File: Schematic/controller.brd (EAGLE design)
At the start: 100 x 80 mm, 46 parts, among them IC1 LM1117-3V3, IC2 LMV358SOIC, Q1 16MHZ, Q2 MMBT2222A, Q3 FDN740P, U1 MC34063SMD, U2 ATMEGA328P

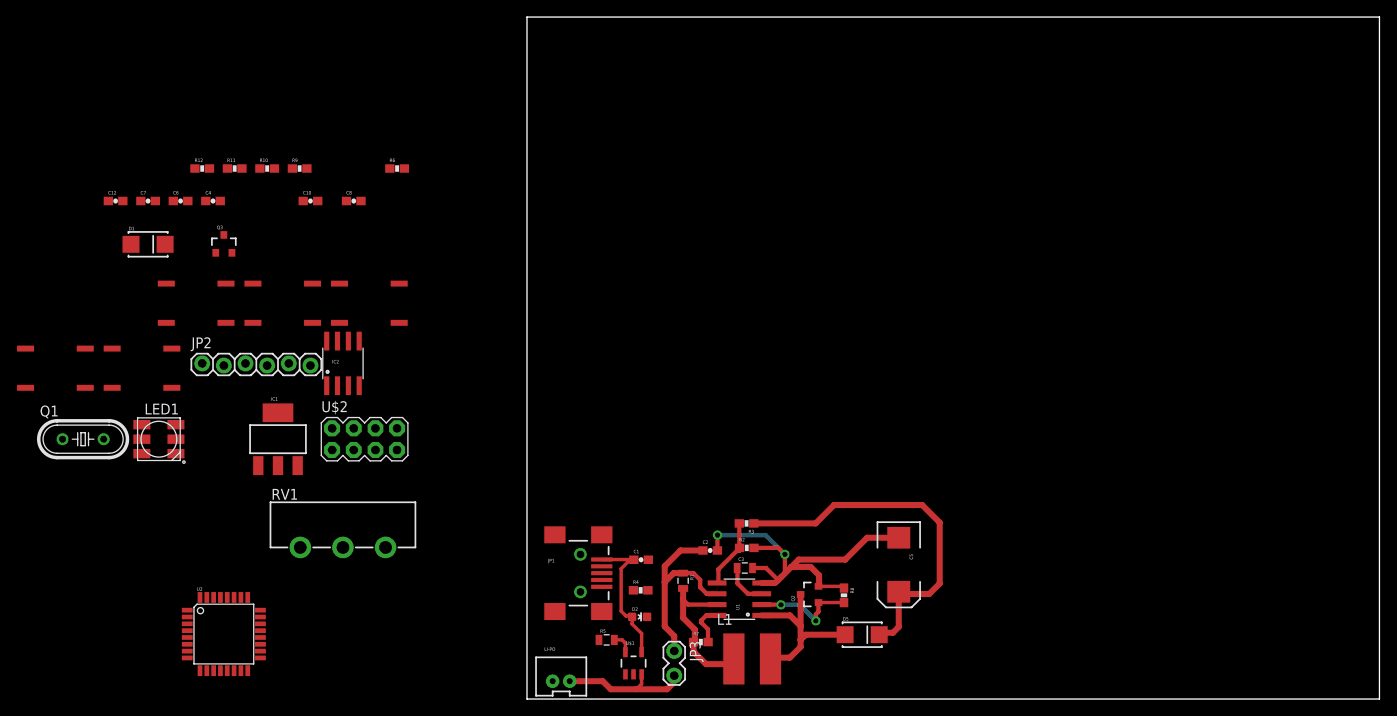
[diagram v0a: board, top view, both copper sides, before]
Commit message: Completed layout for the controller
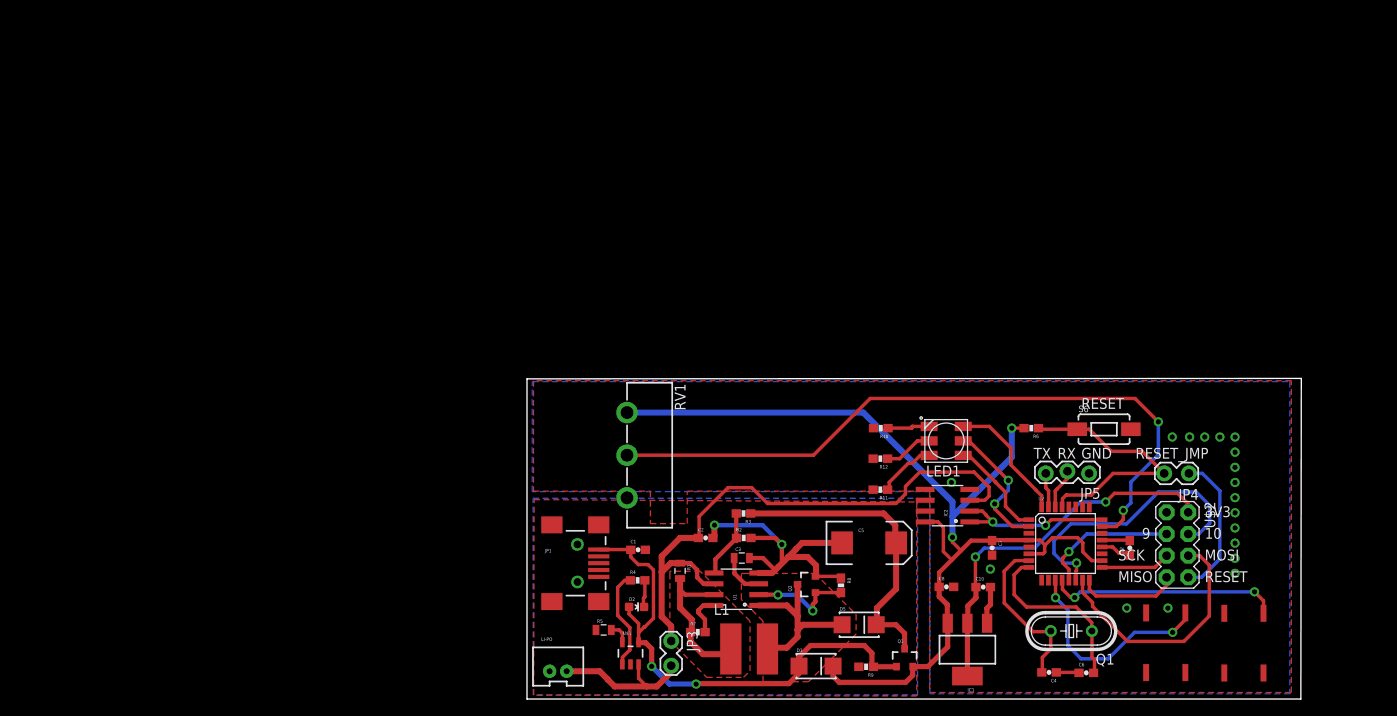
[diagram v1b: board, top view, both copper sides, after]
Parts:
- removed JP2: SERIAL CONN, SparkFun-Connectors:1X06_LOCK
- removed S1, S2, S3: SMD-TACT-SWITCH-4, Misc:SMD-TACTSWITCH-6X6X3
- added JP4: M02LOCK, SparkFun-Connectors:1X02_LOCK
- added JP5: (no value), SparkFun-Connectors:1X03_LOCK
- added S6: SWITCH-MOMENTARY-2SMD-1101NE, SparkFun-Electromechanical:TACTILE-SWITCH-1101NE
- moved S5 135.1 mm to (87.2, 9.65), turned to 270 degrees
- moved C12 125.7 mm to (70.7, 17.7), turned to 90 degrees
- moved C6 119.8 mm to (65.6, 3.07)
- moved Q1 118.1 mm to (63.9, 7.98), turned to 180 degrees
- moved S4 116.8 mm to (78.0, 9.70), turned to 270 degrees
- moved C4 112.6 mm to (61.2, 3.12), turned to 180 degrees
- moved C7 107.0 mm to (54.6, 17.7), turned to 270 degrees
- moved U2 99.3 mm to (63.2, 18.2)
- moved U$2 96.2 mm to (76.3, 18.1), turned to 270 degrees
- moved Q3 93.5 mm to (44.3, 4.80)
- moved D1 92.7 mm to (33.9, 3.86)
- moved LED1 92.4 mm to (49.2, 30.3), turned to 180 degrees
- moved C10 91.0 mm to (53.5, 13.1)
- moved R9 88.5 mm to (39.8, 3.78), turned to 180 degrees
- moved R12 86.5 mm to (41.5, 28.2), turned to 180 degrees
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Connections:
- net N$1 renamed PWR_L2
- net N$12 renamed PWR_L1
- removed net N$2: C2.1, JP3.1, R1.1, U1.6
- removed net VCC: D1.A
- new net V_BAT_SENSE: C2.1, IC2.3, JP3.1, R1.1, U1.6
- net 5V_REG: no longer Q3.1, R9.1
- net GND: now also C12.2, JP5.1, S6.2; no longer JP2.1, S1.P$2, S2.P$2, S3.P$2
- net IO5: no longer S2.P$1
- net IO6: no longer S3.P$1
- net MCU_RXD: now also JP5.2; no longer JP2.4
- net MCU_TXD: now also JP5.3, U2.31; no longer JP2.5
- net N$21: now also JP4.1
- net N$8: now also JP4.2, S6.1; no longer S1.P$1
- net V_BAT: no longer IC2.3
- net V_USB: now also D1.A, Q3.1, R9.1
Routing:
- net 5V_REG: track 0.00 -> 122.7 mm, vias 0 -> 2
- net AD0: track 0.00 -> 82.2 mm, vias 0 -> 2
- net V_BAT_SENSE: track 0.00 -> 68.7 mm
- net 3V3: track 0.00 -> 44.5 mm, vias 0 -> 2
- net V_USB: track 16.8 -> 59.6 mm, vias 0 -> 2
- net IO10: track 0.00 -> 33.0 mm, vias 0 -> 1
- net N$8: track 0.00 -> 31.1 mm
- net MOSI: track 0.00 -> 29.1 mm
- net IO8: track 0.00 -> 27.2 mm, vias 0 -> 2
- net IO7: track 0.00 -> 25.4 mm, vias 0 -> 2
- net N$2: track 23.7 -> 0.00 mm
- net N$7: track 0.00 -> 20.9 mm
- net N$3: track 0.00 -> 19.3 mm
- net AD1: track 0.00 -> 19.2 mm, vias 0 -> 2
- net N$21: track 0.00 -> 17.1 mm
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- added copper zone on layer 1, net GND
- added copper zone on layer 16, net GND
- added copper zone on layer 1, net PWR_L1
- added copper zone on layer 1, net PWR_L2
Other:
- board size 100 x 80 mm -> 90.8 x 37.6 mm
- board text added: "10"
- board text added: "3V3"
- board text added: "9"
- board text added: "GND"
- board text added: "MISO"
- board text added: "MOSI"
- board text added: "RESET"
- board text added: "RESET_JMP"
- board text added: "RX"
- board text added: "SCK"
- board text added: "TX"
